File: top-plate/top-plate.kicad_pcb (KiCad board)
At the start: 2 copper layers, 57.2 x 57.2 mm, 0 parts

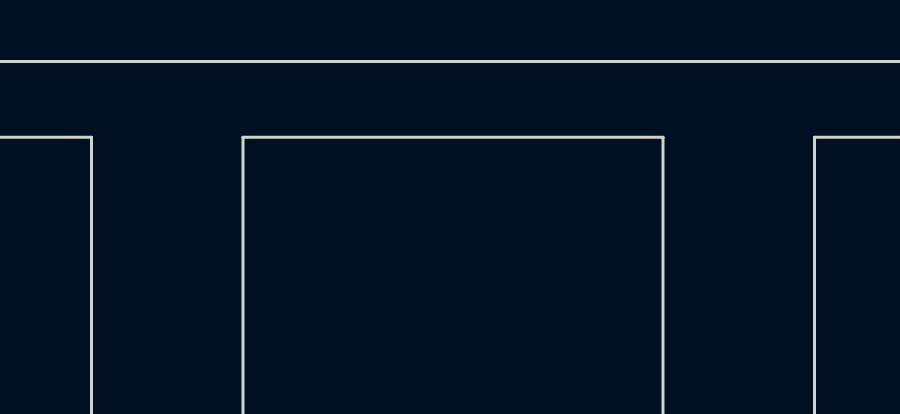
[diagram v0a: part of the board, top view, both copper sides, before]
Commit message: Add placeholder label for JLC order
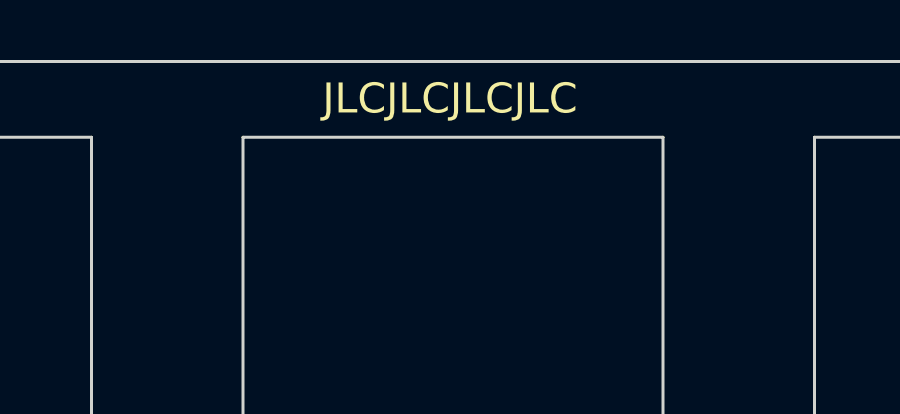
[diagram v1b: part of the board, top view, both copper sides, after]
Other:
- board text added: "JLCJLCJLCJLC"
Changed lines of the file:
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@@
       (layerselection 0x00010fc_ffffffff)
       (disableapertmacros false)
-      (usegerberextensions false)
+      (usegerberextensions true)
       (usegerberattributes true)
       (usegerberadvancedattributes true)
-      (creategerberjobfile true)
+      (creategerberjobfile false)
       (svguseinch false)
       (svgprecision 6)
@@
       (psa4output false)
       (plotreference true)
-      (plotvalue true)
+      (plotvalue false)
       (plotinvisibletext false)
       (sketchpadsonfab false)
@@
   (gr_line (start 137.3 115.589204) (end 123.3 115.589204) (layer "Edge.Cuts") (width 0.1))
   (gr_line (start 161.4 96.539204) (end 161.4 82.539204) (layer "Edge.Cuts") (width 0.1))
+  (gr_text "JLCJLCJLCJLC" (at 149.25 81.25) (layer "F.SilkS")
+    (effects (font (size 1 1) (thickness 0.15)))
+  )
 )
